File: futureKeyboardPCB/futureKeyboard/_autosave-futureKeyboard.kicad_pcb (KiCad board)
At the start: 2 copper layers, 106 parts, among them J1 Conn_01x01, J10 Conn_01x02, J11 Conn_01x01, J12 Conn_01x01, J13 Conn_01x04, J14 Conn_01x06, J15 Conn_01x06, J16 Conn_01x01, J2 Conn_01x04, J3 Conn_01x01, J4 Conn_01x01, J5 Conn_01x04, J6 Conn_01x06, J7 Conn_01x06, J8 Conn_01x01, J9 Conn_01x01, P1 CONN_01X02, P2 CONN_01X06, P3 CONN_01X02, P4 CONN_01X06, Q1 2SC1815, Q2 2SC1815, Q3 2SC1815, Q4 2SC1815, Q5 2SC1815, Q6 2SC1815, SW1 SW_SPDT, SW10 SW_Push, SW11 SW_Push, SW12 SW_Push, SW13 SW_Push, SW14 SW_Push, SW15 SW_Push, SW16 SW_Push, SW17 SW_Push, SW18 SW_Push, SW19 SW_Push, SW2 SW_Push, SW20 SW_Push, SW21 SW_Push, SW22 SW_Push, SW23 SW_Push, SW24 SW_Push, SW25 SW_Push, SW3 SW_Push, SW4 SW_Push, SW5 SW_Push, SW6 SW_Push, SW7 SW_Push, SW8 SW_Push, SW9 SW_SPDT, U1 AMS1117-1.5, U2 ESP32, U3 AMS1117-1.5, U4 ESP32

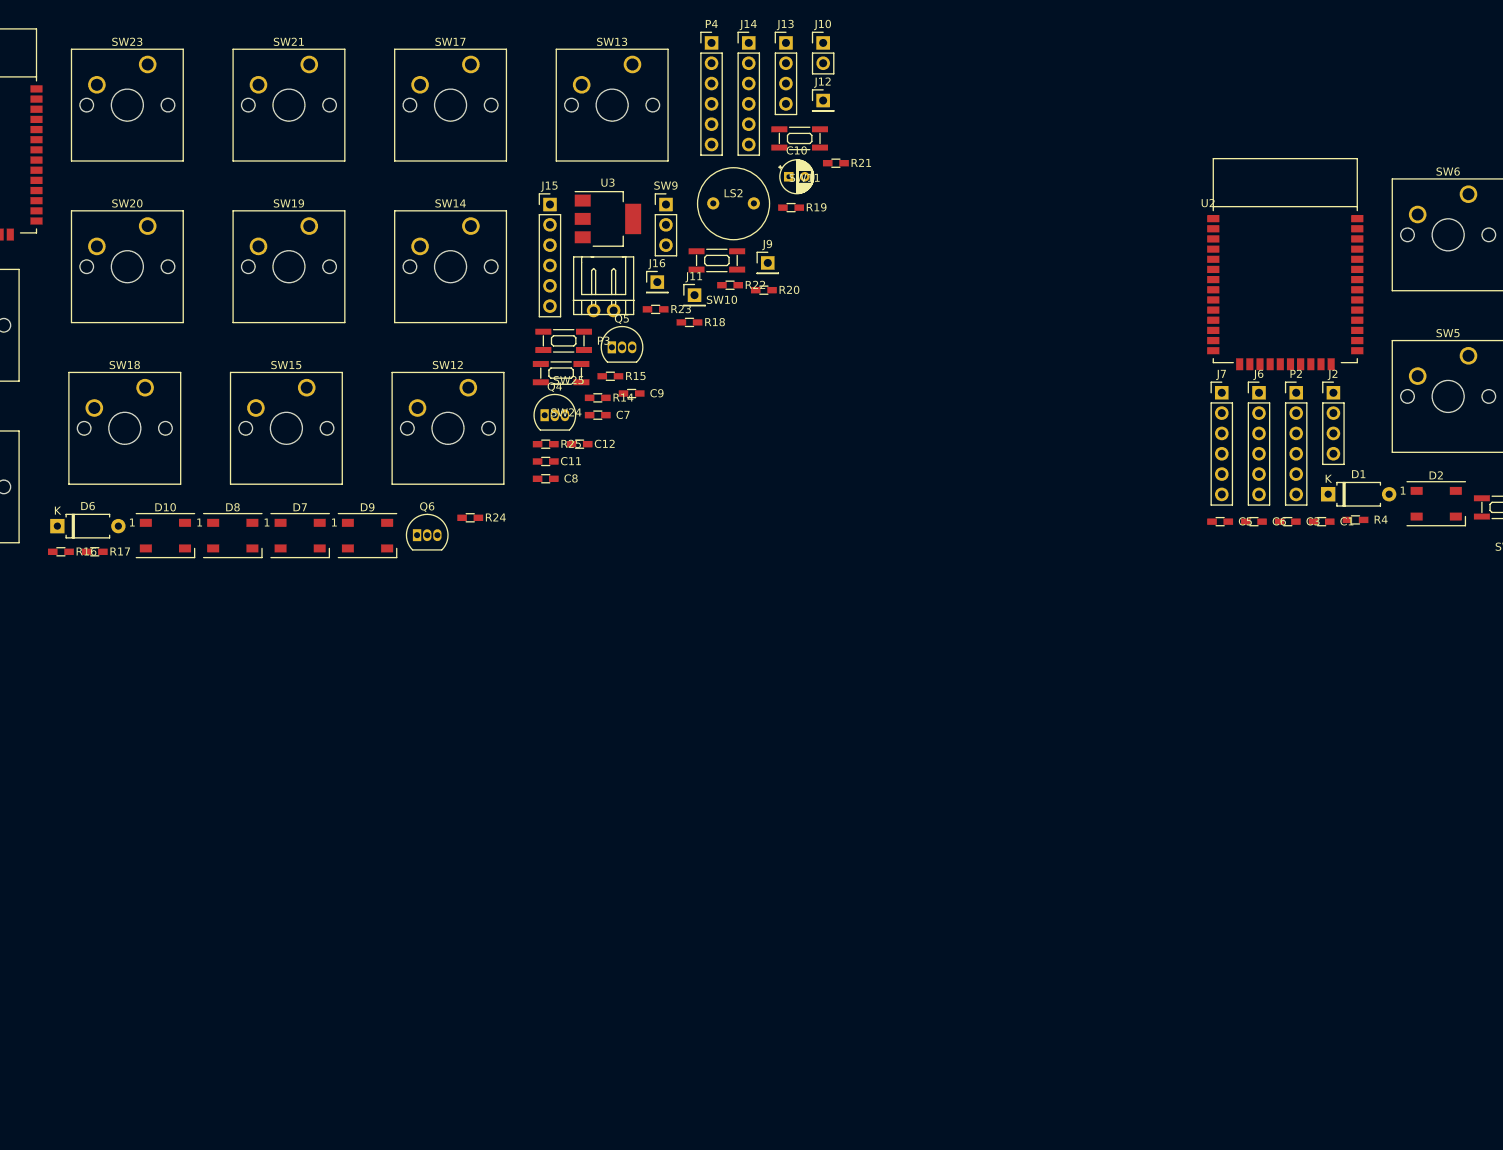
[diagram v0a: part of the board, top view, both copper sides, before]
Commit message: fix netlist, and make PCB file
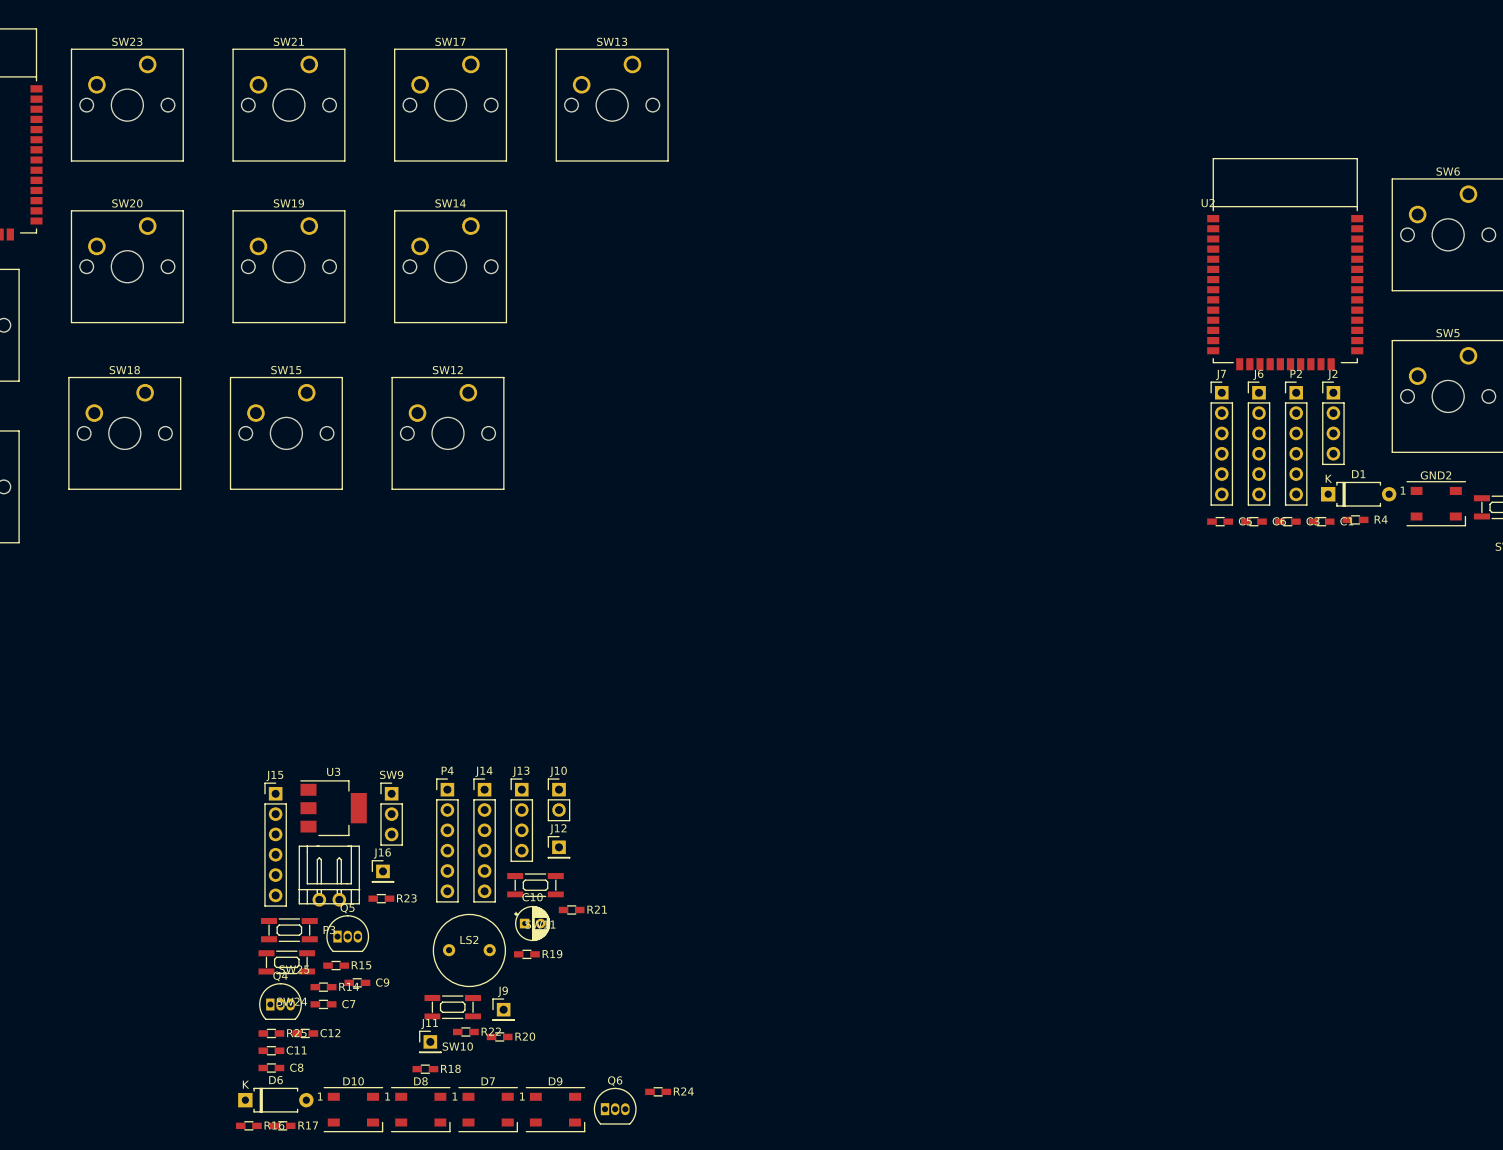
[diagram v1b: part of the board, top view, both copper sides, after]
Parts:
- moved C10 99.0 mm to (98.8, 128.4)
- moved J10 99.0 mm to (103.1, 111.7)
- moved J11 99.0 mm to (87.0, 143.2)
- moved J12 99.0 mm to (103.1, 118.9)
- moved J13 99.0 mm to (98.5, 111.7)
- moved J14 99.0 mm to (93.8, 111.7)
- moved J9 99.0 mm to (96.2, 139.2)
- moved LS2 99.0 mm to (91.9, 131.8)
- moved P4 99.0 mm to (89.2, 111.7)
- moved R18 99.0 mm to (86.4, 146.6)
- moved R19 99.0 mm to (99.1, 132.3)
- moved R20 99.0 mm to (95.7, 142.6)
- moved R21 99.0 mm to (104.7, 126.7)
- moved SW10 99.0 mm to (87.3, 140.0)
- moved R22 99.0 mm to (91.5, 142.0)
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- renumbered D2 to GND2
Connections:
- C1 pad 2: GND -> /Sheet5F548957/GND2
- C10 pad 2: GND -> /Sheet5F548F88/GND
- C11 pad 2: GND -> /Sheet5F548F88/GND
- C12 pad 1: GND -> /Sheet5F548F88/GND
- C2 pad 2: GND -> /Sheet5F548957/GND2
- C3 pad 2: GND -> /Sheet5F548957/GND2
- C4 pad 2: GND -> /Sheet5F548957/GND2
- C5 pad 2: GND -> /Sheet5F548957/GND2
- C6 pad 1: GND -> /Sheet5F548957/GND2
- C7 pad 2: GND -> /Sheet5F548F88/GND
- C8 pad 2: GND -> /Sheet5F548F88/GND
- C9 pad 2: GND -> /Sheet5F548F88/GND
- D10 pad 3: GND -> /Sheet5F548F88/GND
- D3 pad 3: GND -> /Sheet5F548957/GND
- D4 pad 3: GND -> /Sheet5F548957/GND
- D5 pad 3: GND -> /Sheet5F548957/GND
- D7 pad 3: GND -> /Sheet5F548F88/GND
- D8 pad 3: GND -> /Sheet5F548F88/GND
- D9 pad 3: GND -> /Sheet5F548F88/GND
- GND2 pad 3: GND -> /Sheet5F548957/GND
- J13 pad 2: GND -> /Sheet5F548F88/GND
- J14 pad 3: GND -> /Sheet5F548F88/GND
- J15 pad 3: GND -> /Sheet5F548F88/GND
- J16 pad 1: GND -> /Sheet5F548F88/GND
- J5 pad 2: GND -> /Sheet5F548957/GND2
- J6 pad 3: GND -> /Sheet5F548957/GND2
- J7 pad 3: GND -> /Sheet5F548957/GND2
- J8 pad 1: GND -> /Sheet5F548957/GND2
- P1 pad 1: GND -> /Sheet5F548957/GND2
- P2 pad 6: GND -> /Sheet5F548957/GND2
- P3 pad 1: GND -> /Sheet5F548F88/GND
- P4 pad 6: GND -> /Sheet5F548F88/GND
- Q3 pad 1: GND -> /Sheet5F548957/GND2
- Q6 pad 1: GND -> /Sheet5F548F88/GND
- R19 pad 2: GND -> /Sheet5F548F88/GND
- R20 pad 2: GND -> /Sheet5F548F88/GND
- R21 pad 2: GND -> /Sheet5F548F88/GND
- R22 pad 2: GND -> /Sheet5F548F88/GND
- R23 pad 2: GND -> /Sheet5F548F88/GND
- R24 pad 1: GND -> /Sheet5F548F88/GND
- R25 pad 1: GND -> /Sheet5F548F88/GND
- R6 pad 2: GND -> /Sheet5F548957/GND2
- RV1 pad 3: GND -> /Sheet5F548957/GND2
- RV2 pad 3: GND -> /Sheet5F548957/GND2
- SW10 pad 1: GND -> /Sheet5F548F88/GND
- SW11 pad 1: GND -> /Sheet5F548F88/GND
- SW2 pad 1: GND -> /Sheet5F548957/GND2
- SW3 pad 1: GND -> /Sheet5F548957/GND2
- SW4 pad 2: GND -> /Sheet5F548957/GND2
- SW5 pad 2: GND -> /Sheet5F548957/GND2
- SW6 pad 2: GND -> /Sheet5F548957/GND2
- SW7 pad 2: GND -> /Sheet5F548957/GND2
- SW8 pad 2: GND -> /Sheet5F548957/GND2
- U1 pad 1: GND -> /Sheet5F548957/GND2
- U2 pad 1: GND -> /Sheet5F548957/GND2
- U2 pad 15: GND -> /Sheet5F548957/GND2
- U2 pad 38: GND -> /Sheet5F548957/GND2
- U3 pad 1: GND -> /Sheet5F548F88/GND
- U4 pad 1: GND -> /Sheet5F548F88/GND
- U4 pad 15: GND -> /Sheet5F548F88/GND
- U4 pad 38: GND -> /Sheet5F548F88/GND
